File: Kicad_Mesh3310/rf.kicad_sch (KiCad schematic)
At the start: 7 parts, among them J2 ANT_A, J3 ANT_B, U2 Ai-Thinker-Ra-01H

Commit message: Cleaning and placing
Cleaning and placing components
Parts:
- AE2: footprint mesh3310:Texas_SWRA416_868MHz_915MHz_right -> mesh3310_footprints:Texas_SWRA416_868MHz_915MHz_right_v2
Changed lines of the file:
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@@
 			)
 		)
-		(property "Footprint" "mesh3310:Texas_SWRA416_868MHz_915MHz_right"
+		(property "Footprint" "mesh3310_footprints:Texas_SWRA416_868MHz_915MHz_right_v2"
 			(at 167.64 71.12 0)
 			(effects

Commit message: Start of routing
Component placing and start off routing
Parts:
- C26: footprint Capacitor_SMD:C_0603_1608Metric -> Capacitor_SMD:C_0402_1005Metric
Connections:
- net VCC_SW renamed +3V3
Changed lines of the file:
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@@
+	)
+	(symbol
+		(lib_id "power:+3V3")
+		(at 125.73 72.39 0)
+		(unit 1)
+		(exclude_from_sim no)
+		(in_bom yes)
+		(on_board yes)
+		(dnp no)
+		(fields_autoplaced yes)
+		(property "Reference" "#PWR011"
+			(at 125.73 76.2 0)
+			(effects
+				(font
+					(size 1.27 1.27)
+				)
+				(hide yes)
+			)
+		)
+		(property "Value" "+3V3"
+			(at 125.73 67.31 0)
+			(effects
+				(font
+					(size 1.27 1.27)
+				)
+			)
+		)
+		(property "Footprint" ""
+			(at 125.73 72.39 0)
+			(effects
+				(font
+					(size 1.27 1.27)
+				)
+				(hide yes)
+			)
+		)
+		(property "Datasheet" ""
+			(at 125.73 72.39 0)
+			(effects
+				(font
+					(size 1.27 1.27)
+				)
+				(hide yes)
+			)
+		)
+		(property "Description" "Power symbol creates a global label with name \"+3V3\""
+			(at 125.73 72.39 0)
+			(effects
+				(font
+					(size 1.27 1.27)
+				)
+				(hide yes)
+			)
+		)
+		(pin "1"
+		)
+		(instances
+			(project "Mesh3310"
+				(path "/8d65c5ef-7a02-4454-aee5-ab9c49e4aeab/d4d7259f-52be-4eaa-97bd-35f544c05202"
+					(reference "#PWR011")
+					(unit 1)
+				)
+			)
+		)
 	)
 	(symbol
@@
 			)
 		)
-		(property "Footprint" "Capacitor_SMD:C_0603_1608Metric"
+		(property "Footprint" "Capacitor_SMD:C_0402_1005Metric"
 			(at 158.75 82.55 0)
 			(effects
@@
 					(unit 1)
 				)
-			)
-		)
-	)
-	(symbol
-		(lib_id "power:+3V3")
-		(at 125.73 72.39 0)
-		(unit 1)
-		(exclude_from_sim no)
-		(in_bom yes)
-		(on_board yes)
-		(dnp no)
-		(fields_autoplaced yes)
-		(property "Reference" "#PWR079"
-			(at 125.73 76.2 0)
-			(effects
-				(font
-					(size 1.27 1.27)
-				)
-				(hide yes)
-			)
-		)
-		(property "Value" "VCC_SW"
-			(at 125.73 67.31 0)
-			(effects
-				(font
-					(size 1.27 1.27)
-				)
-			)
-		)
-		(property "Footprint" ""
-			(at 125.73 72.39 0)
-			(effects
-				(font
-					(size 1.27 1.27)
-				)
-				(hide yes)
-			)
-		)
-		(property "Datasheet" ""
-			(at 125.73 72.39 0)
-			(effects
-				(font
-					(size 1.27 1.27)
-				)
-				(hide yes)
-			)
-		)
-		(property "Description" "Power symbol creates a global label with name \"+3V3\""
-			(at 125.73 72.39 0)
-			(effects
-				(font
-					(size 1.27 1.27)
-				)
-				(hide yes)
-			)
-		)
-		(pin "1"
-		)
-		(instances
-			(project "Mesh3310"
-				(path "/8d65c5ef-7a02-4454-aee5-ab9c49e4aeab/d4d7259f-52be-4eaa-97bd-35f544c05202"
-					(reference "#PWR079")
-					(unit 1)
-				)

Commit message: backup work
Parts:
- removed AE2: Antenna_Dipole, mesh3310_footprints:Texas_SWRA416_868MHz_915MHz_right_v2, symbol Device:Antenna
- removed FL1: LFCN-1000+, Filter:Filter_Mini-Circuits_FV1206, symbol RF_Filter:LFCN-490
- removed J2: ANT_A, TestPoint:TestPoint_Pad_D1.5mm, symbol Connector:Conn_01x01_Pin
- removed J3: ANT_B, TestPoint:TestPoint_Pad_D1.5mm, symbol Connector:Conn_01x01_Pin
- added ANT1: 0868AT43A0020E, mesh3310_footprints:XCVR_0868AT43A0020E, symbol 0868AT43A0020E:0868AT43A0020E
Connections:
- net at U2.1 (ANT): now also ANT1.1 (FEED)

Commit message: cleanup
schematic cleanup
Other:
- moved on the sheet: C25, C26

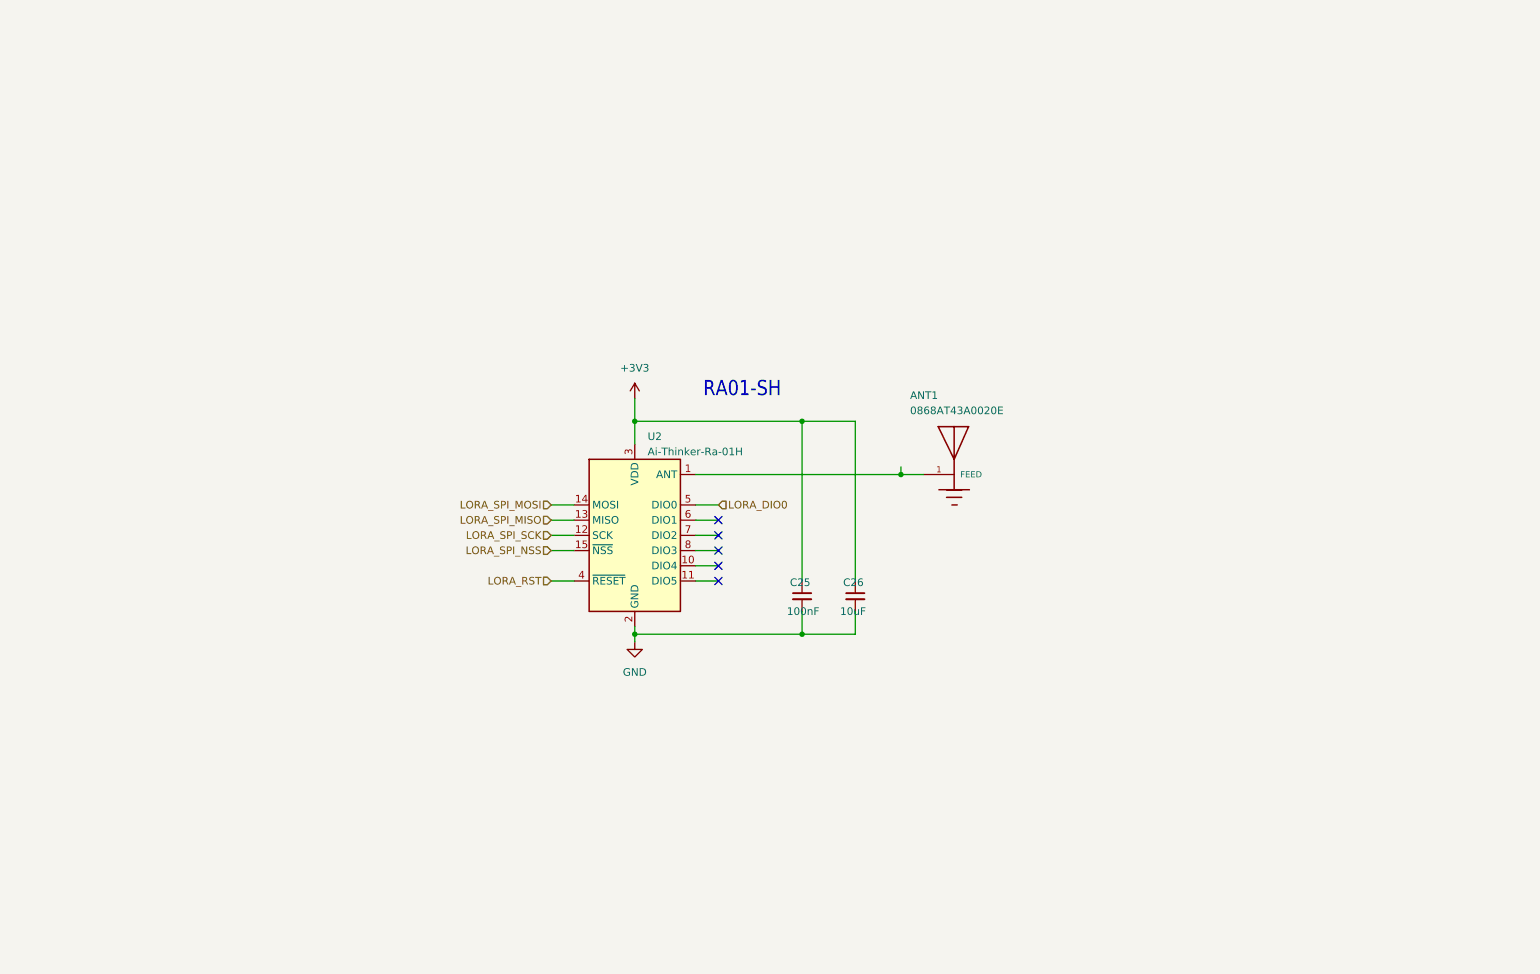
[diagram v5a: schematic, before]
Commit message: Lora changes
Schematic changes to from RA to SOC
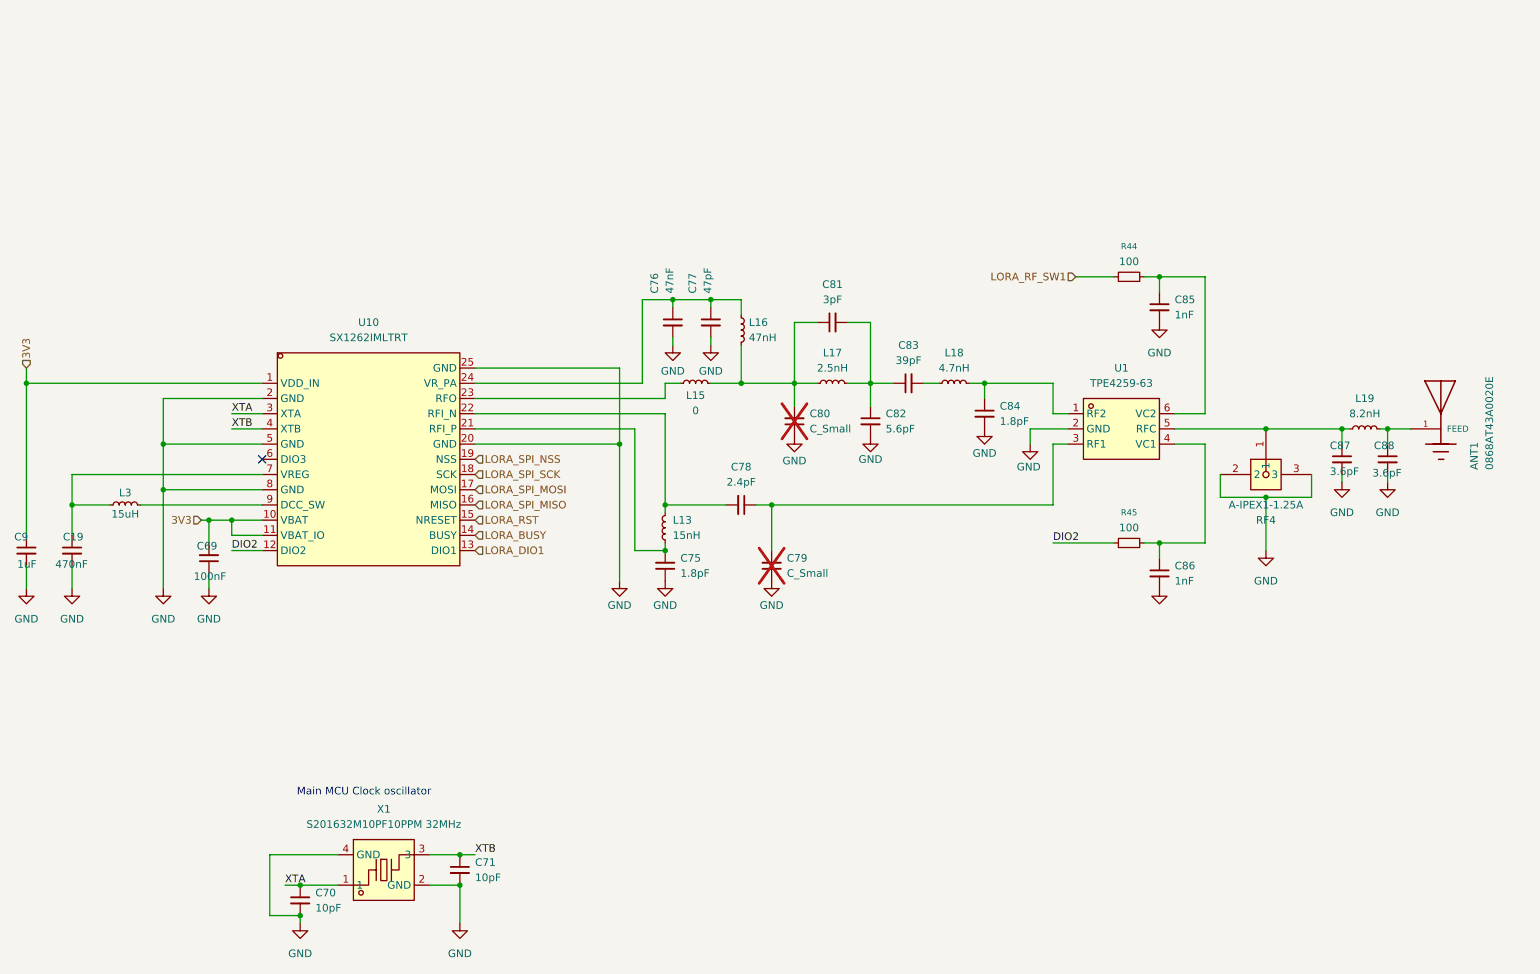
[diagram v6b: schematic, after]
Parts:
- removed C25: 100nF, Capacitor_SMD:C_0402_1005Metric, symbol Device:C_Small
- removed C26: 10uF, Capacitor_SMD:C_0402_1005Metric, symbol Device:C_Small
- removed U2: Ai-Thinker-Ra-01H, RF_Module:Ai-Thinker-Ra-01-LoRa, symbol RF_Module:Ai-Thinker-Ra-01
- added C19: 470nF, Capacitor_SMD:C_0603_1608Metric, symbol Device:C_Small
- added C69: 100nF, Capacitor_SMD:C_0402_1005Metric, symbol Device:C_Small
- added C70, C71: 10pF, Capacitor_SMD:C_0402_1005Metric, symbol Device:C_Small
- added C75, C84: 1.8pF, Capacitor_SMD:C_0402_1005Metric, symbol Device:C_Small
- added C76: 47nF, Capacitor_SMD:C_0402_1005Metric, symbol Device:C_Small
- added C77: 47pF, Capacitor_SMD:C_0402_1005Metric, symbol Device:C_Small
- added C78: 2.4pF, Capacitor_SMD:C_0402_1005Metric, symbol Device:C_Small
- added C79, C80: C_Small, Capacitor_SMD:C_0402_1005Metric, symbol Device:C_Small
- added C81: 3pF, Capacitor_SMD:C_0402_1005Metric, symbol Device:C_Small
- added C82: 5.6pF, Capacitor_SMD:C_0402_1005Metric, symbol Device:C_Small
- added C83: 39pF, Capacitor_SMD:C_0402_1005Metric, symbol Device:C_Small
- added C85, C86: 1nF, Capacitor_SMD:C_0402_1005Metric, symbol Device:C_Small
- added C87, C88: 3.6pF, Capacitor_SMD:C_0402_1005Metric, symbol Device:C_Small
- added C9: 1uF, Capacitor_SMD:C_0603_1608Metric, symbol Device:C_Small
- added L13: 15nH, Inductor_SMD:L_0402_1005Metric, symbol Device:L_Small
- added L15: 0, Inductor_SMD:L_0402_1005Metric, symbol Device:L_Small
- added L16: 47nH, Inductor_SMD:L_0402_1005Metric, symbol Device:L_Small
- added L17: 2.5nH, Inductor_SMD:L_0402_1005Metric, symbol Device:L_Small
- added L18: 4.7nH, Inductor_SMD:L_0402_1005Metric, symbol Device:L_Small
- added L19: 8.2nH, Inductor_SMD:L_0402_1005Metric, symbol Device:L_Small
- added L3: 15uH, Inductor_SMD:L_0603_1608Metric, symbol Device:L_Small
- added R44, R45: 100, Resistor_SMD:R_0402_1005Metric, symbol Device:R_Small
- added RF4: A-IPEX1-1.25A, mesh3310_footprints:IPEX-SMD_3P-L2.6-W2.6-LS3.0_RF1200001R, symbol lcsc:A-IPEX1-1.25A
- added U1: TPE4259-63, mesh3310_footprints:SOT-363-6_L2.0-W1.3-P0.65-LS2.1-BL, symbol lcsc:TPE4259-63
- added U10: SX1262IMLTRT, mesh3310_footprints:QFN-24_L4.0-W4.0-P0.50-BL-EP2.6, symbol lcsc:SX1262IMLTRT
- added X1: S201632M10PF10PPM 32MHz, mesh3310_footprints:CRYSTAL-SMD_4P-L2.0-W1.6-BL, symbol lcsc:S201632M10PF10PPM
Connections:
- net GND: now also C19.2, C69.1, C70.2, C71.2, C75.1, C76.2, C77.2, C79.1, C80.1, C82.2, C84.2, C85.2, C86.2, C87.2, C88.2, C9.2, RF4.2, RF4.3, U1.2 (GND), U10.2 (GND), U10.20 (GND), U10.25 (GND), U10.5 (GND), U10.8 (GND), X1.2 (GND), X1.4 (GND)
- net LORA_RST: now also U10.15 (NRESET)
- net LORA_SPI_MISO: now also U10.16 (MISO)
- net LORA_SPI_MOSI: now also U10.17 (MOSI)
- net LORA_SPI_NSS: now also U10.19 (NSS)
- net LORA_SPI_SCK: now also U10.18 (SCK)
- net at ANT1.1 (FEED): now also C88.1, L19.2
- new net: C81.2, C82.1, C83.1, L17.2
- new net: C83.2, L18.1
- new net: C80.2, C81.1, L15.2, L16.2, L17.1
- new net: C76.1, C77.1, L16.1, U10.24 (VR_PA)
- new net: C75.2, L13.1, U10.21 (RFI_P)
- new net: C78.2, L13.2, U10.22 (RFI_N)
- new net: L15.1, U10.23 (RFO)
- new net: C19.1, L3.1, U10.7 (VREG)
- new net: L3.2, U10.9 (DCC_SW)
- new net: C86.1, R45.2, U1.4 (VC1)
- new net: C87.1, L19.1, RF4.1, U1.5 (RFC)
- new net: C85.1, R44.2, U1.6 (VC2)
- new net: C78.1, C79.2, U1.3 (RF1)
- new net: C84.1, L18.2, U1.1 (RF2)
- new net 3V3: C69.2, C9.1, U10.1 (VDD_IN), U10.10 (VBAT), U10.11 (VBAT_IO)
- new net DIO2: R45.1, U10.12 (DIO2)
- new net LORA_BUSY: U10.14 (BUSY)
- new net LORA_DIO1: U10.13 (DIO1)
- new net LORA_RF_SW1: R44.1
- new net XTA: C70.1, U10.3 (XTA), X1.1
- new net XTB: C71.1, U10.4 (XTB), X1.3
- no-connect marks 5 -> 1
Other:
- note added: "Main MCU Clock oscillator"
- note removed: "RA01-SH"

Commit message: Lora placement
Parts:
- added R6: 0R, Resistor_SMD:R_0402_1005Metric, symbol Device:R_Small
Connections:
- net at RF4.1, U1.5 (RFC): now also R6.1; no longer C87.1, L19.1
- new net: C87.1, L19.1, R6.2
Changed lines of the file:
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@@
 	(wire
 		(pts
+			(xy 231.14 83.82) (xy 234.95 83.82)
+		)
+		(stroke
+			(width 0)
+			(type default)
+		)
+	)
+	(wire
+		(pts
 			(xy 138.43 62.23) (xy 143.51 62.23)
 		)
@@
 	(wire
 		(pts
-			(xy 231.14 83.82) (xy 243.84 83.82)
-		)
-		(stroke
-			(width 0)
-			(type default)
-		)
-	)
-	(wire
-		(pts
 			(xy 24.13 110.49) (xy 24.13 106.68)
 		)
@@
 	(wire
 		(pts
+			(xy 240.03 83.82) (xy 243.84 83.82)
+		)
+		(stroke
+			(width 0)
+			(type default)
+		)
+	)
+	(wire
+		(pts
 			(xy 54.61 99.06) (xy 58.42 99.06)
 		)
@@
 		(length 2.54)
 		(shape diamond)
-		(at 237.49 83.82 0)
+		(at 226.06 83.82 0)
 		(effects
 			(font
@@
 		)
 		(property "Netclass" "LORA-RF"
-			(at 235.458 82.804 90)
+			(at 224.028 82.804 90)
 			(effects
 				(font
@@
 		)
 		(property "Component Class" ""
-			(at 24.13 12.7 0)
+			(at 12.7 12.7 0)
 			(effects
 				(font
@@
 					(unit 1)
 				)
+			)
+		)
+	)
+	(symbol
+		(lib_id "Device:R_Small")
+		(at 237.49 83.82 90)
+		(unit 1)
+		(exclude_from_sim no)
+		(in_bom yes)
+		(on_board yes)
+		(dnp no)
+		(fields_autoplaced yes)
+		(property "Reference" "R6"
+			(at 237.49 78.74 90)
+			(effects
+				(font
+					(size 1.016 1.016)
+				)
+			)
+		)
+		(property "Value" "0R"
+			(at 237.49 81.28 90)
+			(effects
+				(font
+					(size 1.27 1.27)
+				)
+			)
+		)
+		(property "Footprint" "Resistor_SMD:R_0402_1005Metric"
+			(at 237.49 83.82 0)
+			(effects
+				(font
+					(size 1.27 1.27)
+				)
+				(hide yes)
+			)
+		)
+		(property "Datasheet" "https://jlcpcb.com/partdetail/25819-0402WGF1000TCE/C25076"
+			(at 237.49 83.82 0)
+			(effects
+				(font
+					(size 1.27 1.27)
+				)
+				(hide yes)
+			)
+		)
+		(property "Description" "Resistor, small symbol"
+			(at 237.49 83.82 0)
+			(effects
+				(font
+					(size 1.27 1.27)
+				)
+				(hide yes)
+			)
+		)
+		(property "LCSC" "C25076"
+			(at 237.49 83.82 90)
+			(effects
+				(font
+					(size 1.27 1.27)
+				)
+				(hide yes)
+			)
+		)
+		(property "Resource" ""
+			(at 237.49 83.82 90)
+			(effects
+				(font
+					(size 1.27 1.27)
+				)
+				(hide yes)
+			)
+		)
+		(property "pin1" ""
+			(at 237.49 83.82 90)
+			(effects
+				(font
+					(size 1.27 1.27)
+				)
+				(hide yes)
+			)
+		)
+		(property "pin2" ""
+			(at 237.49 83.82 90)
+			(effects
+				(font
+					(size 1.27 1.27)
+				)
+				(hide yes)
+			)
+		)
+		(property "pin3" ""
+			(at 237.49 83.82 90)
+			(effects
+				(font
+					(size 1.27 1.27)
+				)
+				(hide yes)
+			)
+		)
+		(property "pin4" ""
+			(at 237.49 83.82 90)
+			(effects
+				(font
+					(size 1.27 1.27)
+				)
+				(hide yes)
+			)
+		)
+		(property "pin5" ""
+			(at 237.49 83.82 90)
+			(effects
+				(font
+					(size 1.27 1.27)
+				)
+				(hide yes)
+			)
+		)
+		(pin "2"
+		)
+		(pin "1"
+		)
+		(instances
+			(project "Mesh3310"
+				(path "/8d65c5ef-7a02-4454-aee5-ab9c49e4aeab/d4d7259f-52be-4eaa-97bd-35f544c05202"
+					(reference "R6")
+					(unit 1)
+				)
